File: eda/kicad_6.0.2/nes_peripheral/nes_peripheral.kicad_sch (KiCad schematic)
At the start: 57 parts

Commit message: feat: GPIO0/1のアサイン決定
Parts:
- removed SW?: SW_OESEL, symbol Switch:SW_SPDT
- added C? (x2): 0.1u, symbol Device:C_Small
- added J?: AUDIO-JACK-SMD-8P_PJ-3536-L6S_, symbol OPL_Connector:AUDIO-JACK-SMD-8P_PJ-3536-L6S_
- added J?: CONN_JOY1, symbol Connector_Generic:Conn_02x05_Odd_Even
- added J?: CONN_JOY2, symbol Connector_Generic:Conn_02x05_Odd_Even
- added J?: CONN_OESEL, symbol Connector_Generic:Conn_02x03_Odd_Even
- added U?: TXB0104PW, Package_SO:TSSOP-14_4.4x5mm_P0.65mm, symbol Logic_LevelTranslator:TXB0104PW
- added U?: 4021, symbol 4xxx:4021
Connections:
- net GPIO_0_D0 is gone; now on net 3V3_A11: JP1.1 (Pin_1)
- net GPIO_0_D1 is gone; now on net 3V3_O2: JP1.2 (Pin_2)
- net GPIO_0_D10 is gone; now on net 3V3_A2: JP1.13 (Pin_13)
- net GPIO_0_D11 is gone; now on net 3V3_D2: JP1.14 (Pin_14)
- net GPIO_0_D12 is gone; now on net 3V3_R/~{W}: JP1.15 (Pin_15)
- net GPIO_0_D13 is gone; now on net 3V3_~{ROMSEL}: JP1.16 (Pin_16)
- net GPIO_0_D14 is gone; now on net 3V3_~{IRQ}: JP1.17 (Pin_17)
- net GPIO_0_D15 is gone; now on net 3V3_~{WE}: JP1.18 (Pin_18)
- net GPIO_0_D2 is gone; now on net 3V3_A10: JP1.3 (Pin_3)
- net GPIO_0_D24 is gone; now on net 3V3_PA6: JP1.27 (Pin_27)
- net GPIO_0_D25 is gone; now on net 3V3_PA7: JP1.28 (Pin_28)
- net GPIO_0_D26 is gone; now on net 3V3_PA5: JP1.31 (Pin_31)
- net GPIO_0_D27 is gone; now on net 3V3_PA8: JP1.32 (Pin_32)
- net GPIO_0_D28 is gone; now on net 3V3_PA2: JP1.33 (Pin_33)
- net GPIO_0_D29 is gone; now on net 3V3_PA11: JP1.34 (Pin_34)
- net GPIO_0_D3 is gone; now on net 3V3_A12: JP1.4 (Pin_4)
- net GPIO_0_D30 is gone; now on net 3V3_PA1: JP1.35 (Pin_35)
- net GPIO_0_D31 is gone; now on net 3V3_PA12: JP1.36 (Pin_36)
- net GPIO_0_D32 is gone; now on net 3V3_PD1: JP1.37 (Pin_37)
- net GPIO_0_D33 is gone; now on net 3V3_PD6: JP1.38 (Pin_38)
- net GPIO_0_D34 is gone; now on net 3V3_PD2: JP1.39 (Pin_39)
- net GPIO_0_D35 is gone; now on net 3V3_PD5: JP1.40 (Pin_40)
- net GPIO_0_D4 is gone; now on net 3V3_A7: JP1.5 (Pin_5)
- net GPIO_0_D5 is gone; now on net 3V3_D7: JP1.6 (Pin_6)
- net GPIO_0_D6 is gone; now on net 3V3_A6: JP1.7 (Pin_7)
- net GPIO_0_D7 is gone; now on net 3V3_D6: JP1.8 (Pin_8)
- net GPIO_0_D8 is gone; now on net 3V3_A3: JP1.9 (Pin_9)
- net GPIO_0_D9 is gone; now on net 3V3_D3: JP1.10 (Pin_10)
- net GPIO_1_D0 is gone; now on net 3V3_A9: JP2.1 (Pin_1)
- net GPIO_1_D1 is gone; now on net 3V3_A13: JP2.2 (Pin_2)
- net GPIO_1_D10 is gone; now on net 3V3_A0: JP2.13 (Pin_13)
- net GPIO_1_D11 is gone; now on net 3V3_D0: JP2.14 (Pin_14)
- net GPIO_1_D12 is gone; now on net 3V3_~{RD}: JP2.15 (Pin_15)
- net GPIO_1_D13 is gone; now on net 3V3_~{VRAMCS}: JP2.16 (Pin_16)
- net GPIO_1_D14 is gone; now on net 3V3_VRAMA10: JP2.17 (Pin_17)
- net GPIO_1_D15 is gone; now on net 3V3_~{PA13}: JP2.18 (Pin_18)
- net GPIO_1_D16 is gone; now on net 3V3_PA4: JP2.19 (Pin_19)
- net GPIO_1_D17 is gone; now on net 3V3_PA9: JP2.20 (Pin_20)
- net GPIO_1_D18 is gone; now on net 3V3_PA3: JP2.21 (Pin_21)
- net GPIO_1_D19 is gone; now on net 3V3_PA10: JP2.22 (Pin_22)
- net GPIO_1_D2 is gone; now on net 3V3_A8: JP2.3 (Pin_3)
- net GPIO_1_D20 is gone; now on net 3V3_PA0: JP2.23 (Pin_23)
- net GPIO_1_D21 is gone; now on net 3V3_PA13: JP2.24 (Pin_24)
- net GPIO_1_D22 is gone; now on net 3V3_PD0: JP2.25 (Pin_25)
- net GPIO_1_D23 is gone; now on net 3V3_PD7: JP2.26 (Pin_26)
- net GPIO_1_D24 is gone; now on net 3V3_PD3: JP2.27 (Pin_27)
- net GPIO_1_D25 is gone; now on net 3V3_PD4: JP2.28 (Pin_28)
- net GPIO_1_D26 is gone; now on net 3V3_RESERVE0: JP2.31 (Pin_31)
- net GPIO_1_D27 is gone; now on net 3V3_RESERVE1: JP2.32 (Pin_32)
- net GPIO_1_D28 is gone; now on net CART_OE_IN: JP2.33 (Pin_33)
- net GPIO_1_D3 is gone; now on net 3V3_A14: JP2.4 (Pin_4)
- net GPIO_1_D4 is gone; now on net 3V3_A5: JP2.5 (Pin_5)
- net GPIO_1_D5 is gone; now on net 3V3_D5: JP2.6 (Pin_6)
- net GPIO_1_D6 is gone; now on net 3V3_A4: JP2.7 (Pin_7)
- net GPIO_1_D7 is gone; now on net 3V3_D4: JP2.8 (Pin_8)
- net GPIO_1_D8 is gone; now on net 3V3_A1: JP2.9 (Pin_9)
- net GPIO_1_D9 is gone; now on net 3V3_D1: JP2.10 (Pin_10)
- net LED_USER is gone; now on net GPIO_1_D29: D?.2 (A)
- net +3V3: now also C?.1, J?.1 (Pin_1), J?.10 (Pin_10), J?.10 (Pin_10), J?.9 (Pin_9), J?.9 (Pin_9), U?.1 (VCCA)
- net +5V: now also C?.1, U?.14 (VCCB)
- net 3V3_PD3: now also U?.2 (A1)
- net 3V3_PD4: now also U?.3 (A2)
- net 3V3_RESERVE0: now also U?.4 (A3)
- net 3V3_RESERVE1: now also U?.5 (A4)
- net 5V_PD3: now also U?.13 (B1)
- net 5V_PD4: now also U?.12 (B2)
- net 5V_RESERVE0: now also U?.11 (B3)
- net 5V_RESERVE1: now also U?.10 (B4)
- net CART_OE: now also J?.3 (Pin_3), U?.8 (OE)
- net CART_OE_IN: now also J?.5 (Pin_5)
- net GND: now also C?.2, C?.2, J?.1 (Pin_1), J?.1 (Pin_1), J?.2 (Pin_2), J?.2 (Pin_2), J?.2 (Pin_2), J?.4 (Pin_4), J?.6 (Pin_6), U?.7 (GND)
- net GPIO_0_D16 renamed DAC_I2S_BCLK
- net GPIO_0_D17 renamed DAC_I2S_DIN
- net GPIO_0_D18 renamed DAC_I2S_LRCLK
- net GPIO_0_D19 renamed DAC_~{SD_MODE}
- net GPIO_1_D30 renamed 3V3_JOY1_DO
- net 3V3_JOY1_DO: now also J?.3 (Pin_3), J?.4 (Pin_4)
- net GPIO_1_D31 renamed 3V3_JOY2_DO
- net 3V3_JOY2_DO: now also J?.3 (Pin_3), J?.4 (Pin_4)
- net GPIO_1_D32 renamed 3V3_JOY1_P/~{S}
- net 3V3_JOY1_P/~{S}: now also J?.5 (Pin_5), J?.6 (Pin_6)
- net GPIO_1_D33 renamed 3V3_JOY2_P/~{S}
- net 3V3_JOY2_P/~{S}: now also J?.5 (Pin_5), J?.6 (Pin_6)
- net GPIO_1_D34 renamed 3V3_JOY1_CLK
- net 3V3_JOY1_CLK: now also J?.7 (Pin_7), J?.8 (Pin_8)
- net GPIO_1_D35 renamed 3V3_JOY2_CLK
- net 3V3_JOY2_CLK: now also J?.7 (Pin_7), J?.8 (Pin_8)
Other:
- company: (none) -> shinolab
- title: (none) -> nes_peripheral
- moved on the sheet: C?, J?, R?, U?

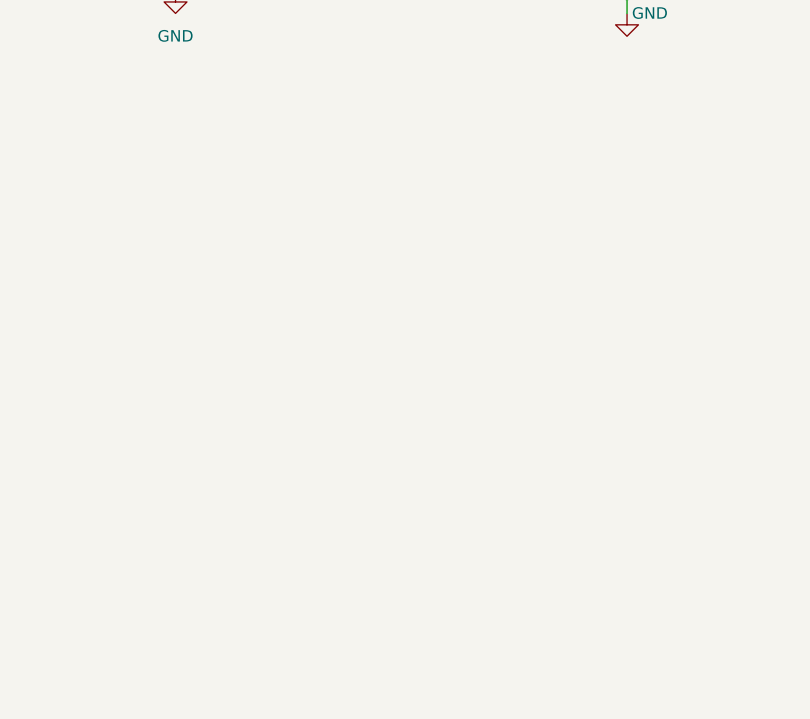
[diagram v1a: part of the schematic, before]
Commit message: feat: MAX98357 のシンボル追加
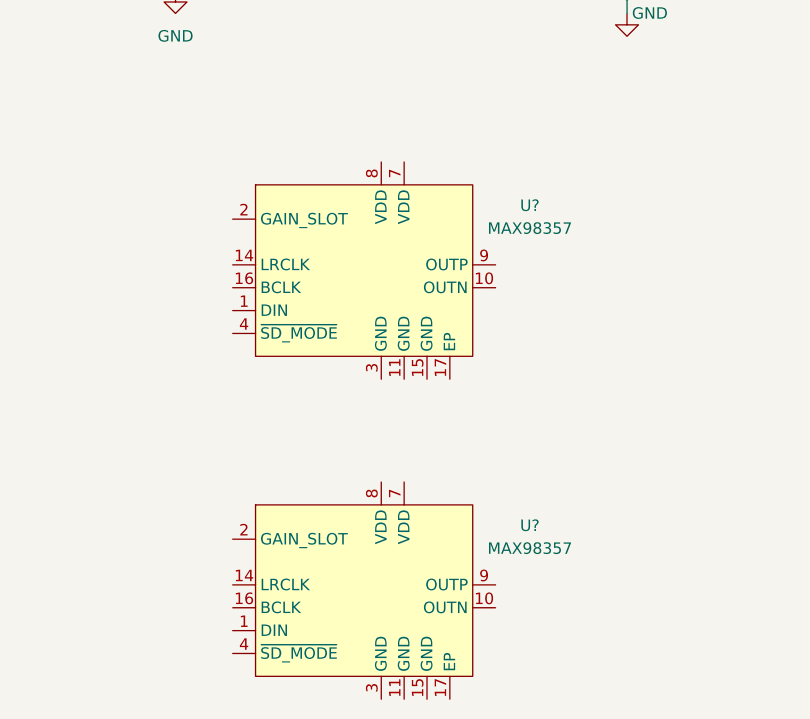
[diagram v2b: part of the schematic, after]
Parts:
- added U? (x2): MAX98357, symbol nes_peripheral:MAX98357
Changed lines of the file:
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@@
     (pin "2")
+  )
+  (symbol (lib_id "nes_peripheral:MAX98357") (at 276.86 384.81 0) (unit 1)
+    (in_bom yes) (on_board yes) (fields_autoplaced)
+    (property "Reference" "U?" (id 0) (at 294.64 376.9612 0))
+    (property "Value" "MAX98357" (id 1) (at 294.64 379.5012 0))
+    (property "Footprint" "" (id 2) (at 276.86 384.81 0)
+      (effects (font (size 1.27 1.27)) hide)
+    )
+    (property "Datasheet" "" (id 3) (at 276.86 384.81 0)
+      (effects (font (size 1.27 1.27)) hide)
+    )
+    (pin "1")
+    (pin "10")
+    (pin "11")
+    (pin "14")
+    (pin "15")
+    (pin "16")
+    (pin "17")
+    (pin "2")
+    (pin "3")
+    (pin "4")
+    (pin "7")
+    (pin "8")
+    (pin "9")
   )
   (symbol (lib_id "Connector_Generic:Conn_02x05_Odd_Even") (at 243.205 309.245 0) (unit 1)
@@
     )
     (pin "1")
+  )
+  (symbol (lib_id "nes_peripheral:MAX98357") (at 276.86 349.25 0) (unit 1)
+    (in_bom yes) (on_board yes) (fields_autoplaced)
+    (property "Reference" "U?" (id 0) (at 294.64 341.4012 0))
+    (property "Value" "MAX98357" (id 1) (at 294.64 343.9412 0))
+    (property "Footprint" "" (id 2) (at 276.86 349.25 0)
+      (effects (font (size 1.27 1.27)) hide)
+    )
+    (property "Datasheet" "" (id 3) (at 276.86 349.25 0)
+      (effects (font (size 1.27 1.27)) hide)
+    )
+    (pin "1")
+    (pin "10")
+    (pin "11")
+    (pin "14")
+    (pin "15")
+    (pin "16")
+    (pin "17")
+    (pin "2")
+    (pin "3")
+    (pin "4")
+    (pin "7")
+    (pin "8")
+    (pin "9")
   )
   (symbol (lib_id "Connector_Generic:Conn_02x20_Odd_Even") (at 71.12 111.76 0) (unit 1)
@@
       (reference "U?") (unit 1) (value "TXB0104PW") (footprint "Package_SO:TSSOP-14_4.4x5mm_P0.65mm")
     )
+    (path "/b150808d-e130-4ef5-a688-8c31e75429df"
+      (reference "U?") (unit 1) (value "MAX98357") (footprint "")
+    )
+    (path "/cf4cf474-89bb-416d-8f2f-9e65aac0a9d3"
+      (reference "U?") (unit 1) (value "MAX98357") (footprint "")
+    )
     (path "/d7a3c763-2fa1-4b71-a156-3fe4743836cb"

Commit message: feat: 音声出力回路を追加
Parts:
- removed J?: AUDIO-JACK-SMD-8P_PJ-3536-L6S_, symbol OPL_Connector:AUDIO-JACK-SMD-8P_PJ-3536-L6S_
- removed U?: MAX98357, symbol nes_peripheral:MAX98357
- added C? (x2): 10p, symbol Device:C_Small
- added C? (x2): 0.1u, symbol Device:C_Small
- added J?: Screw_Terminal_SPK, symbol Connector:Screw_Terminal_01x04
- added J?: CONN_GAINSEL, symbol Connector_Generic:Conn_02x05_Odd_Even
- added J?: CONN_USER, symbol Connector_Generic:Conn_02x05_Odd_Even
- added R?: 0, symbol Device:R_Small
- added R? (x2): 100k, symbol Device:R_Small
- added R?: 330k, symbol Device:R_Small
- added U?: MAX98357, symbol nes_peripheral:MAX98357
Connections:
- net +3V3: now also U?.7 (VDD), U?.8 (VDD), C?.1, C?.1, C?.1, C?.1, J?.1 (Pin_1), J?.2 (Pin_2), J?.8 (Pin_8), R?.2, U?.7 (VDD), U?.8 (VDD)
- net 3V3_RESERVE0: now also J?.7 (Pin_7)
- net 3V3_RESERVE1: now also J?.8 (Pin_8)
- net DAC_I2S_BCLK: now also U?.16 (BCLK), U?.16 (BCLK)
- net DAC_I2S_DIN: now also U?.1 (DIN), U?.1 (DIN)
- net DAC_I2S_LRCLK: now also U?.14 (LRCLK), U?.14 (LRCLK)
- net DAC_~{SD_MODE}: now also R?.2, R?.2
- net GND: now also U?.11 (GND), U?.15 (GND), U?.17 (EP), U?.3 (GND), C?.2, C?.2, C?.2, C?.2, J?.10 (Pin_10), J?.4 (Pin_4), J?.9 (Pin_9), R?.1, U?.11 (GND), U?.15 (GND), U?.17 (EP), U?.3 (GND)
- net GPIO_0_D20: now also J?.3 (Pin_3)
- net GPIO_0_D21: now also J?.4 (Pin_4)
- net GPIO_0_D22: now also J?.5 (Pin_5)
- net GPIO_0_D23: now also J?.6 (Pin_6)
- net at U?.10 (OUTN): now also J?.2 (Pin_2)
- net GAIN_SLOT: now reaches U?.2 (GAIN_SLOT)
- net GAIN_SLOT: now also J?.1 (Pin_1), J?.3 (Pin_3), J?.5 (Pin_5), J?.7 (Pin_7), J?.9 (Pin_9), U?.2 (GAIN_SLOT)
- net at U?.4 (~{SD_MODE}): now also R?.1
- net at U?.9 (OUTP): now also J?.1 (Pin_1)
- new net: J?.4 (Pin_4), U?.10 (OUTN)
- new net: R?.1, U?.4 (~{SD_MODE})
- new net: J?.3 (Pin_3), U?.9 (OUTP)
- new net: J?.2 (Pin_2), R?.1
- new net: J?.10 (Pin_10), R?.2
- no-connect marks 0 -> 1
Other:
- note added: "15dB 12dB 9dB 6dB 3dB"
- moved on the sheet: C?, D?, J?, R?, U?

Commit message: feat: デバッグピン・コントローラの回路を追加
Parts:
- removed J?: CONN_5VSEL, symbol Connector_Generic:Conn_02x03_Odd_Even
- removed J?: CONN_OESEL, symbol Connector_Generic:Conn_02x03_Odd_Even
- added C? (x2): 0.1u, symbol Device:C_Small
- added J?: DB9_Female_JOY1, symbol Connector:DB9_Female
- added J?: CONN_SOUND_IO, symbol Connector_Generic:Conn_02x03_Odd_Even
- added J?: CONN_SPK, symbol Connector_Generic:Conn_02x03_Odd_Even
- added J?: CONN_JOY2_FC, symbol Connector_Generic:Conn_02x15_Top_Bottom
- added J?: DB15_Female_JOY1, symbol Connector:DB15_Female
- added J?: CONN_5V_RESERVE, symbol Connector_Generic:Conn_02x03_Odd_Even
- added J?: CONN_JOY1_MIC, symbol Connector_Generic:Conn_01x02
- added J? (x2): CONN_CART_DBG, symbol Connector_Generic:Conn_01x30
- added J? (x2): CONN_GPIO0_DBG, symbol Connector_Generic:Conn_01x20
- added J? (x2): CONN_GPIO1_DBG, symbol Connector_Generic:Conn_01x20
- added J?: CONN_JOY1_FC_COMPATIBLE, symbol Connector_Generic:Conn_02x09_Top_Bottom
- added J?: DB9_Female_JOY2, symbol Connector:DB9_Female
- added J?: CONN_JOY1_OE_SEL, symbol Connector_Generic:Conn_01x03
- added J?: CONN_JOY1_FC, symbol Connector_Generic:Conn_02x15_Top_Bottom
- added J?: CONN_CART_OE_SEL, symbol Connector_Generic:Conn_01x03
- added J?: DB15_Female_JOY2, symbol Connector:DB15_Female
- added J?: CONN_JOY2_OE_SEL, symbol Connector_Generic:Conn_01x03
- added J?: CONN_JOY2_MIC, symbol Connector_Generic:Conn_01x02
- added J?: CONN_JOY2_FC_COMPATIBLE, symbol Connector_Generic:Conn_02x09_Top_Bottom
- added J?: CONN_5VSEL, symbol Connector_Generic:Conn_01x03
- added R? (x2): 10k, symbol Device:R_Small
- added U?: TXB0104PW, Package_SO:TSSOP-14_4.4x5mm_P0.65mm, symbol Logic_LevelTranslator:TXB0104PW
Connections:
- net +3V3: now also J?.1 (Pin_1), J?.1 (Pin_1), C?.1, J?.1 (Pin_1), J?.1 (Pin_1), J?.1 (Pin_1), J?.15 (Pin_15), J?.15 (Pin_15), J?.3 (Pin_3), U?.1 (VCCA); no longer J?.10 (Pin_10), J?.10 (Pin_10), J?.9 (Pin_9), J?.9 (Pin_9)
- net +5V: now also C?.1, J?.1 (Pin_1), J?.1 (Pin_1), J?.1 (Pin_1), J?.15 (P15), J?.15 (P15), J?.15 (Pin_15), J?.15 (Pin_15), J?.15 (Pin_15), J?.15 (Pin_15), J?.16 (Pin_16), J?.16 (Pin_16), J?.2 (Pin_2), J?.2 (Pin_2), J?.2 (Pin_2), J?.30 (Pin_30), J?.30 (Pin_30), J?.30 (Pin_30), J?.6, J?.6, J?.6 (Pin_6), J?.6 (Pin_6), J?.7, J?.7, J?.7 (Pin_7), J?.7 (Pin_7), U?.14 (VCCB)
- net 3V3_A0: now also J?.7 (Pin_7)
- net 3V3_A1: now also J?.5 (Pin_5)
- net 3V3_A10: now also J?.2 (Pin_2)
- net 3V3_A11: now also J?.1 (Pin_1)
- net 3V3_A12: now also J?.2 (Pin_2)
- net 3V3_A13: now also J?.1 (Pin_1)
- net 3V3_A14: now also J?.2 (Pin_2)
- net 3V3_A2: now also J?.7 (Pin_7)
- net 3V3_A3: now also J?.5 (Pin_5)
- net 3V3_A4: now also J?.4 (Pin_4)
- net 3V3_A5: now also J?.3 (Pin_3)
- net 3V3_A6: now also J?.4 (Pin_4)
- net 3V3_A7: now also J?.3 (Pin_3)
- net 3V3_A8: now also J?.2 (Pin_2)
- net 3V3_A9: now also J?.1 (Pin_1)
- net 3V3_D0: now also J?.7 (Pin_7)
- net 3V3_D1: now also J?.5 (Pin_5)
- net 3V3_D2: now also J?.7 (Pin_7)
- net 3V3_D3: now also J?.5 (Pin_5)
- net 3V3_D4: now also J?.4 (Pin_4)
- net 3V3_D5: now also J?.3 (Pin_3)
- net 3V3_D6: now also J?.4 (Pin_4)
- net 3V3_D7: now also J?.3 (Pin_3)
- net 3V3_JOY1_CLK: now also U?.4 (A3), J?.20 (Pin_20); no longer J?.8 (Pin_8)
- net 3V3_JOY1_DO: now also U?.2 (A1), J?.18 (Pin_18); no longer J?.4 (Pin_4)
- net 3V3_JOY1_P/~{S}: now also U?.3 (A2), J?.19 (Pin_19); no longer J?.6 (Pin_6)
- net 3V3_JOY2_CLK: now also J?.20 (Pin_20), U?.4 (A3); no longer J?.8 (Pin_8)
- net 3V3_JOY2_DO: now also J?.18 (Pin_18), U?.2 (A1); no longer J?.4 (Pin_4)
- net 3V3_JOY2_P/~{S}: now also J?.19 (Pin_19), U?.3 (A2); no longer J?.6 (Pin_6)
- net 3V3_O2: now also J?.1 (Pin_1)
- net 3V3_PA0: now also J?.12 (Pin_12)
- net 3V3_PA1: now also J?.18 (Pin_18)
- net 3V3_PA10: now also J?.11 (Pin_11)
- net 3V3_PA11: now also J?.17 (Pin_17)
- net 3V3_PA12: now also J?.18 (Pin_18)
- net 3V3_PA13: now also J?.12 (Pin_12)
- net 3V3_PA2: now also J?.17 (Pin_17)
- net 3V3_PA3: now also J?.11 (Pin_11)
- net 3V3_PA4: now also J?.10 (Pin_10)
- net 3V3_PA5: now also J?.16 (Pin_16)
- net 3V3_PA6: now also J?.14 (Pin_14)
- net 3V3_PA7: now also J?.14 (Pin_14)
- net 3V3_PA8: now also J?.16 (Pin_16)
- net 3V3_PA9: now also J?.10 (Pin_10)
- net 3V3_PD0: now also J?.13 (Pin_13)
- net 3V3_PD1: now also J?.19 (Pin_19)
- net 3V3_PD2: now also J?.20 (Pin_20)
- net 3V3_PD3: now also J?.14 (Pin_14); no longer U?.2 (A1)
- net 3V3_PD4: now also J?.14 (Pin_14); no longer U?.3 (A2)
- net 3V3_PD5: now also J?.20 (Pin_20)
- net 3V3_PD6: now also J?.19 (Pin_19)
- net 3V3_PD7: now also J?.13 (Pin_13)
- net 3V3_RESERVE0: now also J?.16 (Pin_16); no longer U?.4 (A3)
- net 3V3_RESERVE1: now also J?.16 (Pin_16); no longer U?.5 (A4)
- net 3V3_R/~{W}: now also J?.8 (Pin_8)
- net 3V3_VRAMA10: now also J?.9 (Pin_9)
- net 3V3_~{IRQ}: now also J?.9 (Pin_9)
- net 3V3_~{PA13}: now also J?.9 (Pin_9)
- net 3V3_~{RD}: now also J?.8 (Pin_8)
- net 3V3_~{ROMSEL}: now also J?.8 (Pin_8)
- net 3V3_~{VRAMCS}: now also J?.8 (Pin_8)
- net 3V3_~{WE}: now also J?.9 (Pin_9)
- net 5V_A0: now also J?.13 (Pin_13)
- net 5V_A1: now also J?.12 (Pin_12)
- net 5V_A10: now also J?.3 (Pin_3)
- net 5V_A11: now also J?.2 (Pin_2)
- net 5V_A12: now also J?.3 (Pin_3)
- net 5V_A13: now also J?.4 (Pin_4)
- net 5V_A14: now also J?.5 (Pin_5)
- net 5V_A2: now also J?.11 (Pin_11)
- net 5V_A3: now also J?.10 (Pin_10)
- net 5V_A4: now also J?.9 (Pin_9)
- net 5V_A5: now also J?.8 (Pin_8)
- net 5V_A6: now also J?.7 (Pin_7)
- net 5V_A7: now also J?.6 (Pin_6)
- net 5V_A8: now also J?.5 (Pin_5)
- net 5V_A9: now also J?.4 (Pin_4)
- net 5V_D0: now also J?.13 (Pin_13)
- net 5V_D1: now also J?.12 (Pin_12)
- net 5V_D2: now also J?.11 (Pin_11)
- net 5V_D3: now also J?.10 (Pin_10)
- net 5V_D4: now also J?.9 (Pin_9)
- net 5V_D5: now also J?.8 (Pin_8)
- net 5V_D6: now also J?.7 (Pin_7)
- net 5V_D7: now also J?.6 (Pin_6)
- net 5V_O2: now also J?.2 (Pin_2)
- net 5V_PA0: now also J?.25 (Pin_25)
- net 5V_PA1: now also J?.24 (Pin_24)
- net 5V_PA10: now also J?.23 (Pin_23)
- net 5V_PA11: now also J?.24 (Pin_24)
- net 5V_PA12: now also J?.25 (Pin_25)
- net 5V_PA13: now also J?.26 (Pin_26)
- net 5V_PA2: now also J?.23 (Pin_23)
- net 5V_PA3: now also J?.22 (Pin_22)
- net 5V_PA4: now also J?.21 (Pin_21)
- net 5V_PA5: now also J?.20 (Pin_20)
- net 5V_PA6: now also J?.19 (Pin_19)
- net 5V_PA7: now also J?.20 (Pin_20)
- net 5V_PA8: now also J?.21 (Pin_21)
- net 5V_PA9: now also J?.22 (Pin_22)
- net 5V_PD0: now also J?.26 (Pin_26)
- net 5V_PD1: now also J?.27 (Pin_27)
- net 5V_PD2: now also J?.28 (Pin_28)
- net 5V_PD3: now also J?.29 (Pin_29); no longer U?.13 (B1)
- net 5V_PD4: now also J?.30 (Pin_30); no longer U?.12 (B2)
- net 5V_PD5: now also J?.29 (Pin_29)
- net 5V_PD6: now also J?.28 (Pin_28)
- net 5V_PD7: now also J?.27 (Pin_27)
- net 5V_RESERVE0: now also J?.3 (Pin_3); no longer U?.11 (B3)
- net 5V_RESERVE1: now also J?.4 (Pin_4); no longer U?.10 (B4)
- net 5V_R/~{W}: now also J?.14 (Pin_14)
- net 5V_VRAMA10: now also J?.18 (Pin_18)
- net 5V_~{IRQ}: now also J?.15 (Pin_15)
- net 5V_~{PA13}: now also J?.19 (Pin_19)
- net 5V_~{RD}: now also J?.17 (Pin_17)
- net 5V_~{ROMSEL}: now also J?.14 (Pin_14)
- net 5V_~{VRAMCS}: now also J?.18 (Pin_18)
- net 5V_~{WE}: now also J?.17 (Pin_17)
- net BOARD_5V: now also J?.1 (Pin_1), J?.6 (Pin_6), J?.6 (Pin_6)
- net CART_OE: now also J?.2 (Pin_2); no longer U?.8 (OE)
- net CART_OE_IN: now also JP1.25 (Pin_25), J?.13 (Pin_13), J?.3 (Pin_3); no longer JP2.33 (Pin_33)
- net DAC_I2S_BCLK: now also J?.10 (Pin_10)
- net DAC_I2S_DIN: now also J?.10 (Pin_10)
- net DAC_I2S_LRCLK: now also J?.11 (Pin_11)
- net DAC_~{SD_MODE}: now also J?.11 (Pin_11)
- net EXT_5V: now also J?.3 (Pin_3)
- net GND: now also J?.10 (Pin_10), J?.10 (Pin_10), J?.4 (Pin_4), J?.4 (Pin_4), J?.6 (Pin_6), J?.6 (Pin_6), J?.8 (Pin_8), J?.8 (Pin_8), C?.2, C?.2, J?.1, J?.1, J?.1 (Pin_1), J?.1 (Pin_1), J?.1 (Pin_1), J?.15 (Pin_15), J?.15 (Pin_15), J?.16 (Pin_16), J?.16 (Pin_16), J?.16 (Pin_16), J?.17 (Pin_17), J?.17 (Pin_17), J?.18 (Pin_18), J?.18 (Pin_18), J?.3 (Pin_3), J?.3 (Pin_3), J?.4 (Pin_4), J?.5 (Pin_5), J?.5 (Pin_5), J?.6 (Pin_6), J?.6 (Pin_6), J?.6 (Pin_6), J?.6 (Pin_6), J?.8, J?.8, J?.8 (Pin_8), J?.8 (Pin_8), J?.9, J?.9, J?.9 (Pin_9), J?.9 (Pin_9), R?.2, R?.2, U?.7 (GND); no longer J?.1 (Pin_1), J?.1 (Pin_1)
- net GPIO_0_D20: now also J?.12 (Pin_12)
- net GPIO_0_D21: now also J?.12 (Pin_12)
- net GPIO_0_D23: now also D?.2 (A), J?.13 (Pin_13); no longer J?.6 (Pin_6)
- net SOUND_I: now also J?.15 (Pin_15), J?.3 (Pin_3)
- net SOUND_O: now also J?.16 (Pin_16), J?.4 (Pin_4)
- net SPK_OUT_R_N: now reaches J?.4 (Pin_4), U?.10 (OUTN)
- net SPK_OUT_R_N: now also J?.6 (Pin_6)
- net SPK_OUT_R_P: now reaches J?.3 (Pin_3), U?.9 (OUTP)
- net SPK_OUT_R_P: now also J?.5 (Pin_5)
- net SPK_OUT_L_P: now reaches J?.1 (Pin_1), U?.9 (OUTP)
- net SPK_OUT_L_P: now also J?.1 (Pin_1)
- net SPK_OUT_L_N: now reaches J?.2 (Pin_2), U?.10 (OUTN)
- net SPK_OUT_L_N: now also J?.2 (Pin_2)
- net GPIO_0_D22 renamed USER_GPIO2
- net USER_GPIO2: no longer JP1.25 (Pin_25)
- net GPIO_1_D29 renamed 3V3_JOY2_MICIN
- net 3V3_JOY2_MICIN: now also J?.9 (Pin_9), J?.17 (Pin_17), U?.5 (A4); no longer D?.2 (A)
- new net: J?.2 (Pin_2), U?.10 (B4) (x2)
- new net 3V3_JOY1_RESERVE: J?.17 (Pin_17), J?.9 (Pin_9), JP2.33 (Pin_33), U?.5 (A4)
- new net 5V_JOY1_CLK: J?.13 (Pin_13), J?.14 (P14), J?.14 (Pin_14), J?.29 (Pin_29), J?.4, J?.4 (Pin_4), U?.11 (B3)
- new net 5V_JOY1_DO: J?.11 (Pin_11), J?.13 (P13), J?.13 (Pin_13), J?.2, J?.2 (Pin_2), J?.28 (Pin_28), U?.13 (B1)
- new net 5V_JOY1_P/~{S}: J?.12 (P12), J?.12 (Pin_12), J?.12 (Pin_12), J?.27 (Pin_27), J?.3, J?.3 (Pin_3), U?.12 (B2)
- new net 5V_JOY1_RESERVE: J?.1 (Pin_1), J?.17 (Pin_17), J?.2, J?.2 (Pin_2)
- new net 5V_JOY2_CLK: J?.13 (Pin_13), J?.14 (P14), J?.14 (Pin_14), J?.29 (Pin_29), J?.4, J?.4 (Pin_4), U?.11 (B3)
- new net 5V_JOY2_DO: J?.11 (Pin_11), J?.13 (P13), J?.13 (Pin_13), J?.2, J?.2 (Pin_2), J?.28 (Pin_28), U?.13 (B1)
- new net 5V_JOY2_MICIN: J?.1 (Pin_1), J?.17 (Pin_17), J?.2, J?.2 (Pin_2)
- new net 5V_JOY2_P/~{S}: J?.12 (P12), J?.12 (Pin_12), J?.12 (Pin_12), J?.27 (Pin_27), J?.3, J?.3 (Pin_3), U?.12 (B2)
- new net JOY1_OE_5V: J?.2 (Pin_2), R?.1, U?.8 (OE)
- new net JOY2_OE_5V: J?.2 (Pin_2), R?.1, U?.8 (OE)
- new net USER_GPIO3: J?.6 (Pin_6)
- no-connect marks 1 -> 67
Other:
- note added: "5V Serial 3V3 Parallel"
- note added: "Always Enable GPIO"
- note added: "BOARD EXT"
- moved on the sheet: C?, D?, J?, R?, U?

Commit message: feat: コントローラのパラレル入力でバッグ回路を追加
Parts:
- removed J?: CONN_USER, symbol Connector_Generic:Conn_02x05_Odd_Even
- added C? (x2): 0.1u, symbol Device:C_Small
- added J?: CONN_JOY1_DBG, symbol Connector_Generic:Conn_02x09_Top_Bottom
- added J?: CONN_JOY2_DBG, symbol Connector_Generic:Conn_02x09_Top_Bottom
- added J?: CONN_USER, symbol Connector_Generic:Conn_02x06_Odd_Even
- added J?: CONN_JOY1_DBGSEL, symbol Connector_Generic:Conn_01x02
- added J?: CONN_JOY2_DBGSEL, symbol Connector_Generic:Conn_01x02
- added R? (x16): 10k, symbol Device:R_Small
- added U?: 4021, symbol 4xxx:4021
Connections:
- net +3V3: now also U?.16 (VDD), C?.1, C?.1, J?.1 (Pin_1), J?.9 (Pin_9), J?.9 (Pin_9), R?.1, R?.1, R?.1, R?.1, R?.1, R?.1, R?.1, R?.1, R?.1, R?.1, R?.1, R?.1, R?.1, R?.1, R?.1, R?.1, U?.16 (VDD)
- net 3V3_JOY1_CLK: now also U?.10 (CP)
- net 3V3_JOY1_DO: now also J?.2 (Pin_2)
- net 3V3_JOY1_P/~{S}: now also U?.9 (PL)
- net 3V3_JOY2_CLK: now also U?.10 (CP)
- net 3V3_JOY2_DO: now also J?.2 (Pin_2)
- net 3V3_JOY2_P/~{S}: now also U?.9 (PL)
- net GND: now also U?.11 (DS), U?.8 (VSS), C?.2, C?.2, J?.10 (Pin_10), J?.10 (Pin_10), J?.11 (Pin_11), J?.11 (Pin_11), J?.12 (Pin_12), J?.12 (Pin_12), J?.13 (Pin_13), J?.13 (Pin_13), J?.14 (Pin_14), J?.14 (Pin_14), J?.15 (Pin_15), J?.15 (Pin_15), J?.16 (Pin_16), J?.16 (Pin_16), J?.17 (Pin_17), J?.17 (Pin_17), J?.18 (Pin_18), J?.18 (Pin_18), J?.4 (Pin_4), U?.11 (DS), U?.8 (VSS)
- net GPIO_0_D20: now also J?.5 (Pin_5), J?.6 (Pin_6)
- net GPIO_0_D21: now also J?.7 (Pin_7), J?.8 (Pin_8)
- net USER_GPIO2: now also J?.10 (Pin_10), J?.9 (Pin_9)
- net USER_GPIO3: now also J?.11 (Pin_11), J?.12 (Pin_12)
- net JOY1_3V3_DBG_D7: now reaches U?.1 (D7)
- net JOY1_3V3_DBG_D7: now also J?.8 (Pin_8), R?.2
- net JOY1_3V3_DBG_D4: now reaches U?.13 (D4)
- net JOY1_3V3_DBG_D4: now also J?.5 (Pin_5), R?.2
- net JOY1_3V3_DBG_D5: now reaches U?.14 (D5)
- net JOY1_3V3_DBG_D5: now also J?.6 (Pin_6), R?.2
- net JOY1_3V3_DBG_D6: now reaches U?.15 (D6)
- net JOY1_3V3_DBG_D6: now also J?.7 (Pin_7), R?.2
- net at U?.3 (Q7): now also J?.1 (Pin_1)
- net JOY1_3V3_DBG_D3: now reaches U?.4 (D3)
- net JOY1_3V3_DBG_D3: now also J?.4 (Pin_4), R?.2
- net JOY1_3V3_DBG_D2: now reaches U?.5 (D2)
- net JOY1_3V3_DBG_D2: now also J?.3 (Pin_3), R?.2
- net JOY1_3V3_DBG_D1: now reaches U?.6 (D1)
- net JOY1_3V3_DBG_D1: now also J?.2 (Pin_2), R?.2
- net JOY1_3V3_DBG_D0: now reaches U?.7 (D0)
- net JOY1_3V3_DBG_D0: now also J?.1 (Pin_1), R?.2
- new net: J?.1 (Pin_1), U?.3 (Q7)
- new net JOY2_3V3_DBG_D0: J?.1 (Pin_1), R?.2, U?.7 (D0)
- new net JOY2_3V3_DBG_D1: J?.2 (Pin_2), R?.2, U?.6 (D1)
- new net JOY2_3V3_DBG_D2: J?.3 (Pin_3), R?.2, U?.5 (D2)
- new net JOY2_3V3_DBG_D3: J?.4 (Pin_4), R?.2, U?.4 (D3)
- new net JOY2_3V3_DBG_D4: J?.5 (Pin_5), R?.2, U?.13 (D4)
- new net JOY2_3V3_DBG_D5: J?.6 (Pin_6), R?.2, U?.14 (D5)
- new net JOY2_3V3_DBG_D6: J?.7 (Pin_7), R?.2, U?.15 (D6)
- new net JOY2_3V3_DBG_D7: J?.8 (Pin_8), R?.2, U?.1 (D7)
- no-connect marks 67 -> 72
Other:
- moved on the sheet: U?

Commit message: fix: ERCを通した
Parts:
- added F1: Polyfuse_Small, symbol Device:Polyfuse_Small
- gave numbers to parts that had none: 123
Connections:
- net EXT_5V: now also F1.1; no longer J4.1
- net GND: now also J1.3 (Pin_3)
- new net: F1.2, J4.1
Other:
- note added: "Cartridge"
- note added: "Cartridge Level-shift"
- note added: "D-class Amp"
- note added: "GPIO"
- note added: "Joypad 3V3 Parallel"
- note added: "Joypad 3V3 Serial"
- note added: "Joypad 5V Serial"
- note added: "Supply, Debug"
- moved on the sheet: J4, J7, J8, R4
